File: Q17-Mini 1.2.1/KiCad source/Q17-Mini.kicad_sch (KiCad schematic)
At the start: 86 parts, among them J1 Input, J2-1 SPK+, J2-2 SPK-, J3-1 V+, J3-2 GND, J3-3 V-, Q1 IRF610, Q10 KSA992, Q11 ZVP2106A, Q12 BD139, Q13 IRF610, Q14 IRF9610, Q15 FQA46N15, Q16 FQA36P15, Q2 KSA992, Q3 KSC1845, Q4 IRF9610, Q5 FQP3P20, Q6 FQP3N30, Q7 KSC1845, Q8 ZVN4206AV, Q9 ZVP2106A, U1 OPA1641

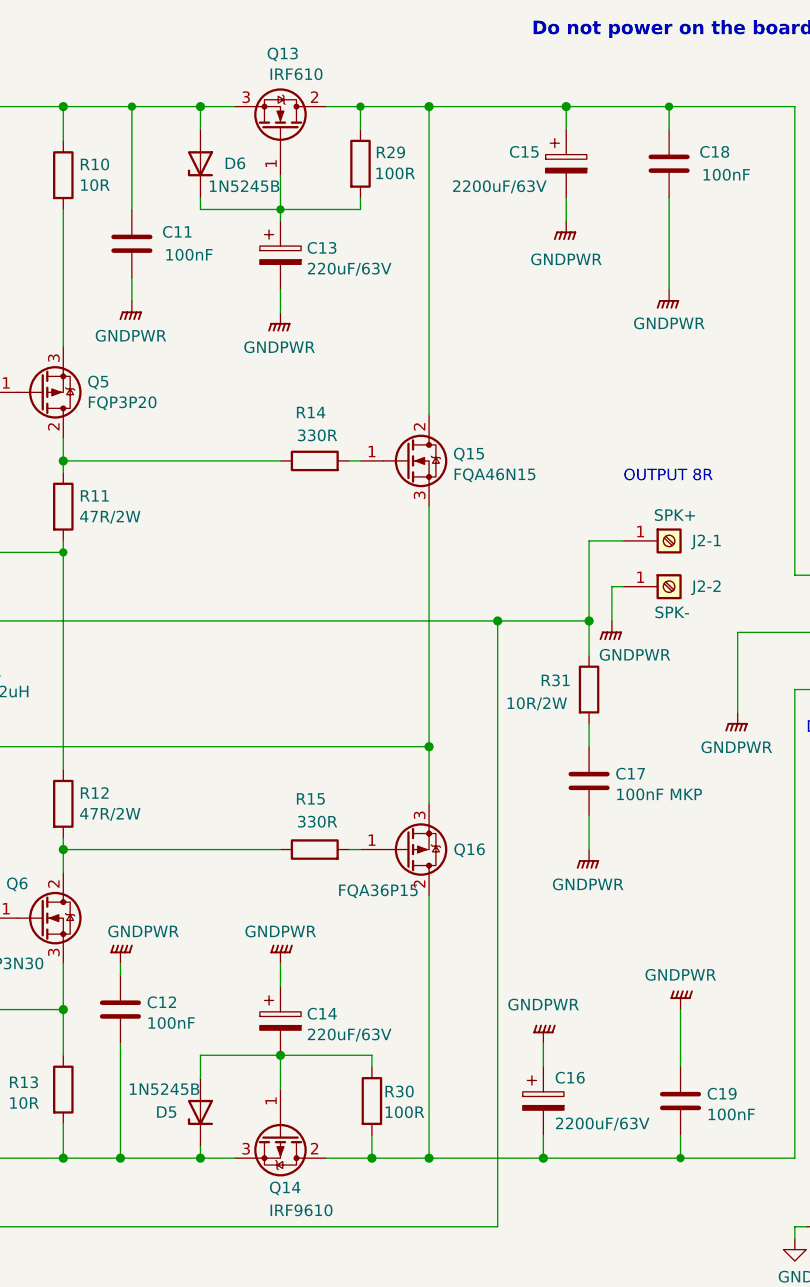
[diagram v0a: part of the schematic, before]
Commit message: Update diagram to 1.3.6
R29/R30 updated to 10k.
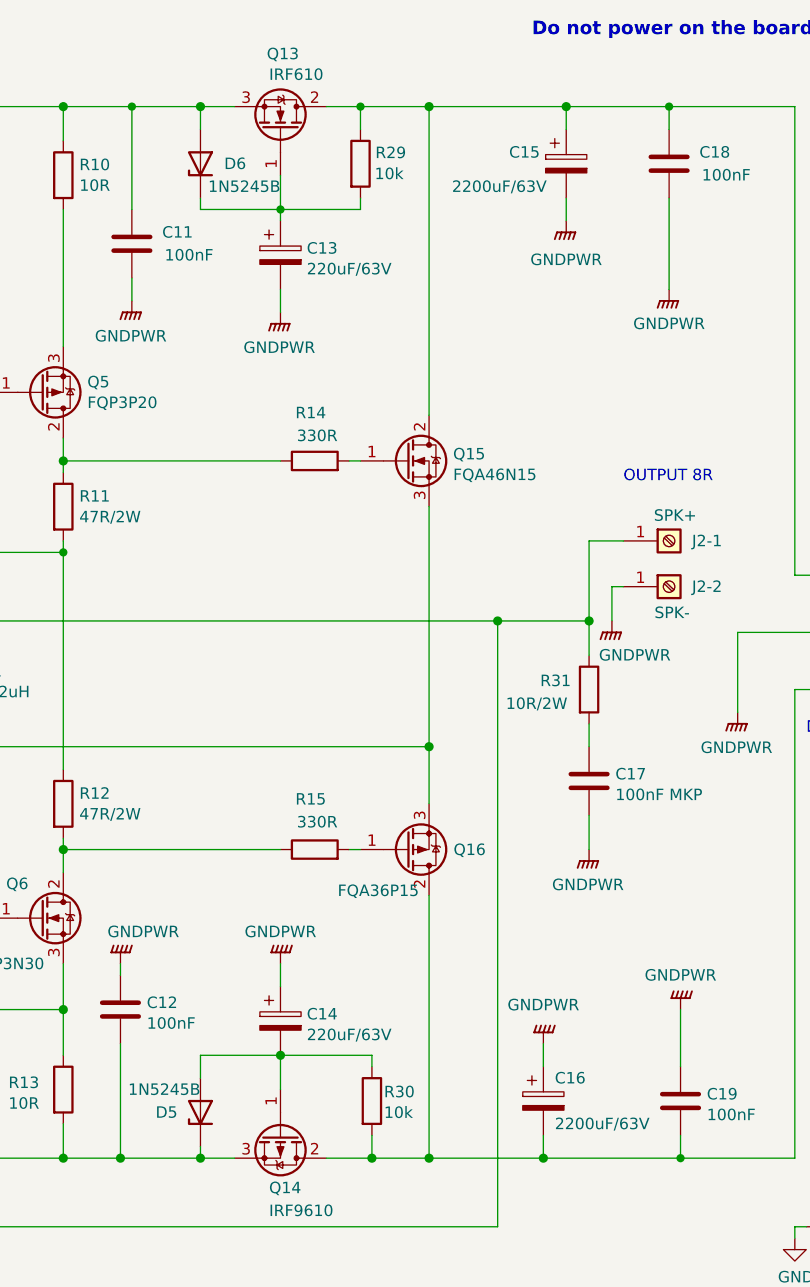
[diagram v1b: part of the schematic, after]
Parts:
- R29, R30: value 100R -> 10k; Part# MRS25000C1000FC100 -> MRS25000C1002FCT00
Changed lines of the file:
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@@
   (title_block
     (title "Q17-Mini Amplifier")
-    (date "2022-08-09")
-    (rev "1.3.5")
+    (date "2022-08-18")
+    (rev "1.3.6")
     (company "by eng. Tiberiu Vicol")
     (comment 1 "Modified by Stef for the Q17-Mini project")
@@
       (effects (font (size 1.27 1.27)) (justify left))
     )
-    (property "Value" "100R" (id 1) (at 216.2005 31.5986 0)
+    (property "Value" "10k" (id 1) (at 216.2005 31.5986 0)
       (effects (font (size 1.27 1.27)) (justify left))
     )
@@
       (effects (font (size 1.27 1.27)) hide)
     )
-    (property "Part#" "MRS25000C1000FC100" (id 4) (at 214.63 30.48 0)
+    (property "Part#" "MRS25000C1002FCT00" (id 4) (at 214.63 30.48 0)
       (effects (font (size 1.27 1.27)) hide)
     )
@@
       (effects (font (size 1.27 1.27)) (justify left))
     )
-    (property "Value" "100R" (id 1) (at 217.2359 135.9102 0)
+    (property "Value" "10k" (id 1) (at 217.2359 135.9102 0)
       (effects (font (size 1.27 1.27)) (justify left))
     )
@@
       (effects (font (size 1.27 1.27)) hide)
     )
-    (property "Part#" "MRS25000C1000FC100" (id 4) (at 215.9 134.62 0)
+    (property "Part#" "MRS25000C1002FCT00" (id 4) (at 215.9 134.62 0)
       (effects (font (size 1.27 1.27)) hide)
     )
@@
     )
     (path "/6a502bca-5c03-4909-9915-ce87906e504a"
-      (reference "R29") (unit 1) (value "100R") (footprint "Resistor_THT:R_Axial_DIN0207_L6.3mm_D2.5mm_P10.16mm_Horizontal")
+      (reference "R29") (unit 1) (value "10k") (footprint "Resistor_THT:R_Axial_DIN0207_L6.3mm_D2.5mm_P10.16mm_Horizontal")
     )
     (path "/860cc2f6-176f-4935-b38a-f52437fa5513"
-      (reference "R30") (unit 1) (value "100R") (footprint "Resistor_THT:R_Axial_DIN0207_L6.3mm_D2.5mm_P10.16mm_Horizontal")
+      (reference "R30") (unit 1) (value "10k") (footprint "Resistor_THT:R_Axial_DIN0207_L6.3mm_D2.5mm_P10.16mm_Horizontal")
     )
     (path "/0b38258b-fc2c-4616-935a-ea7f37c299ab"

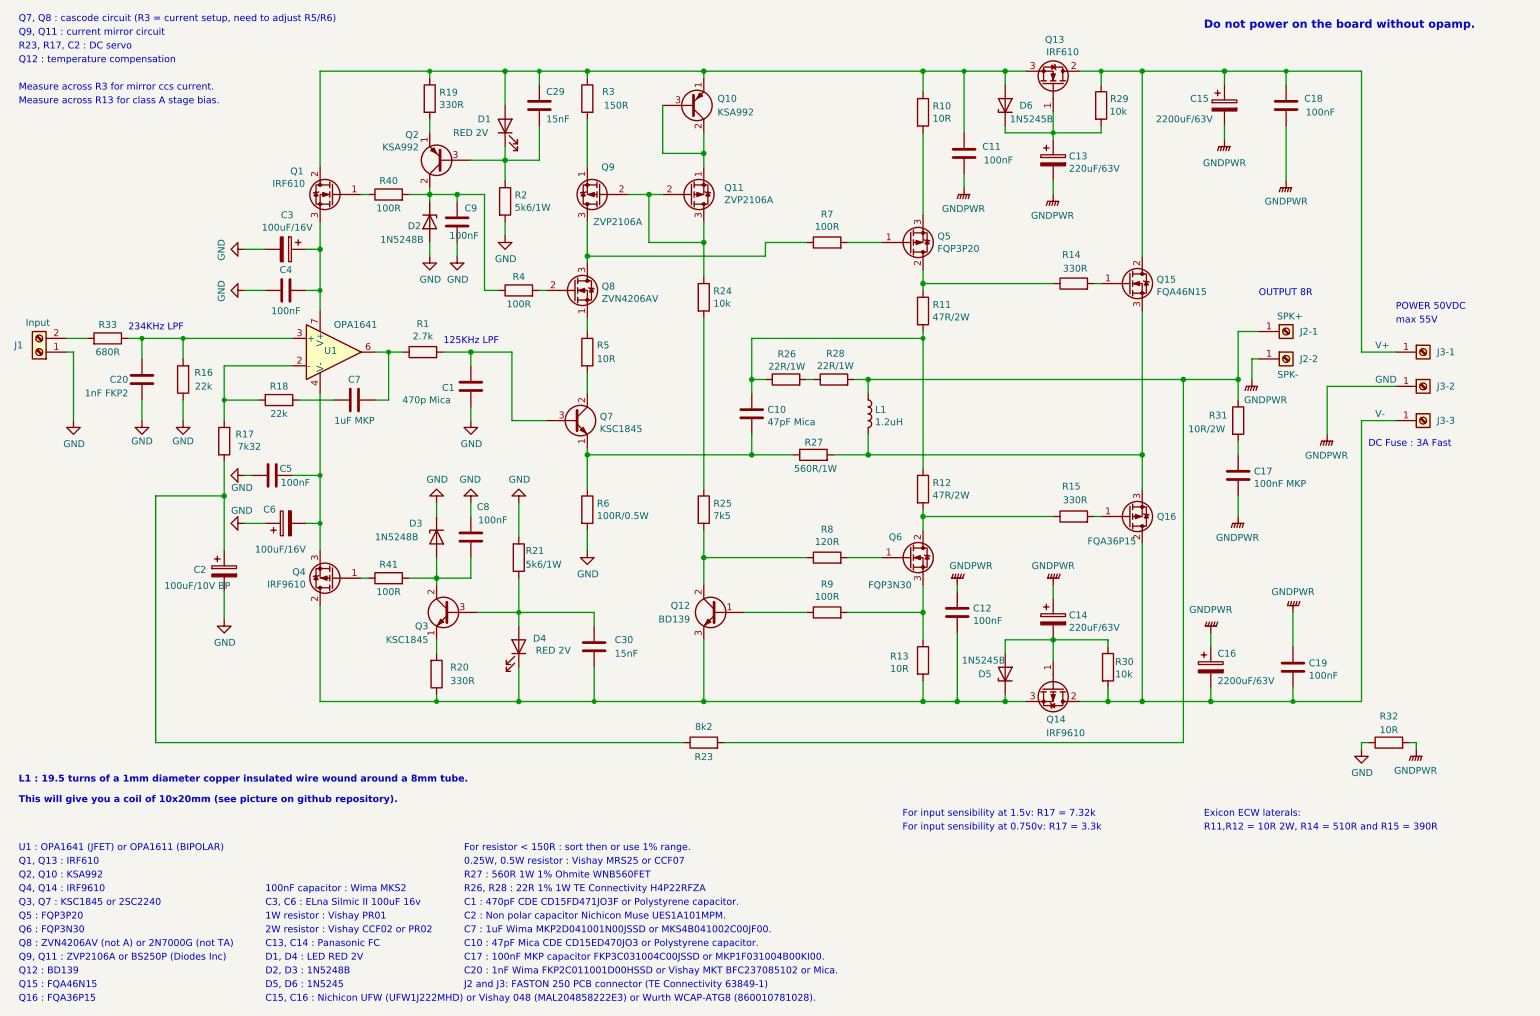
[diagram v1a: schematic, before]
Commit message: Update Q17-Mini 1.2.1
Updated schematic.
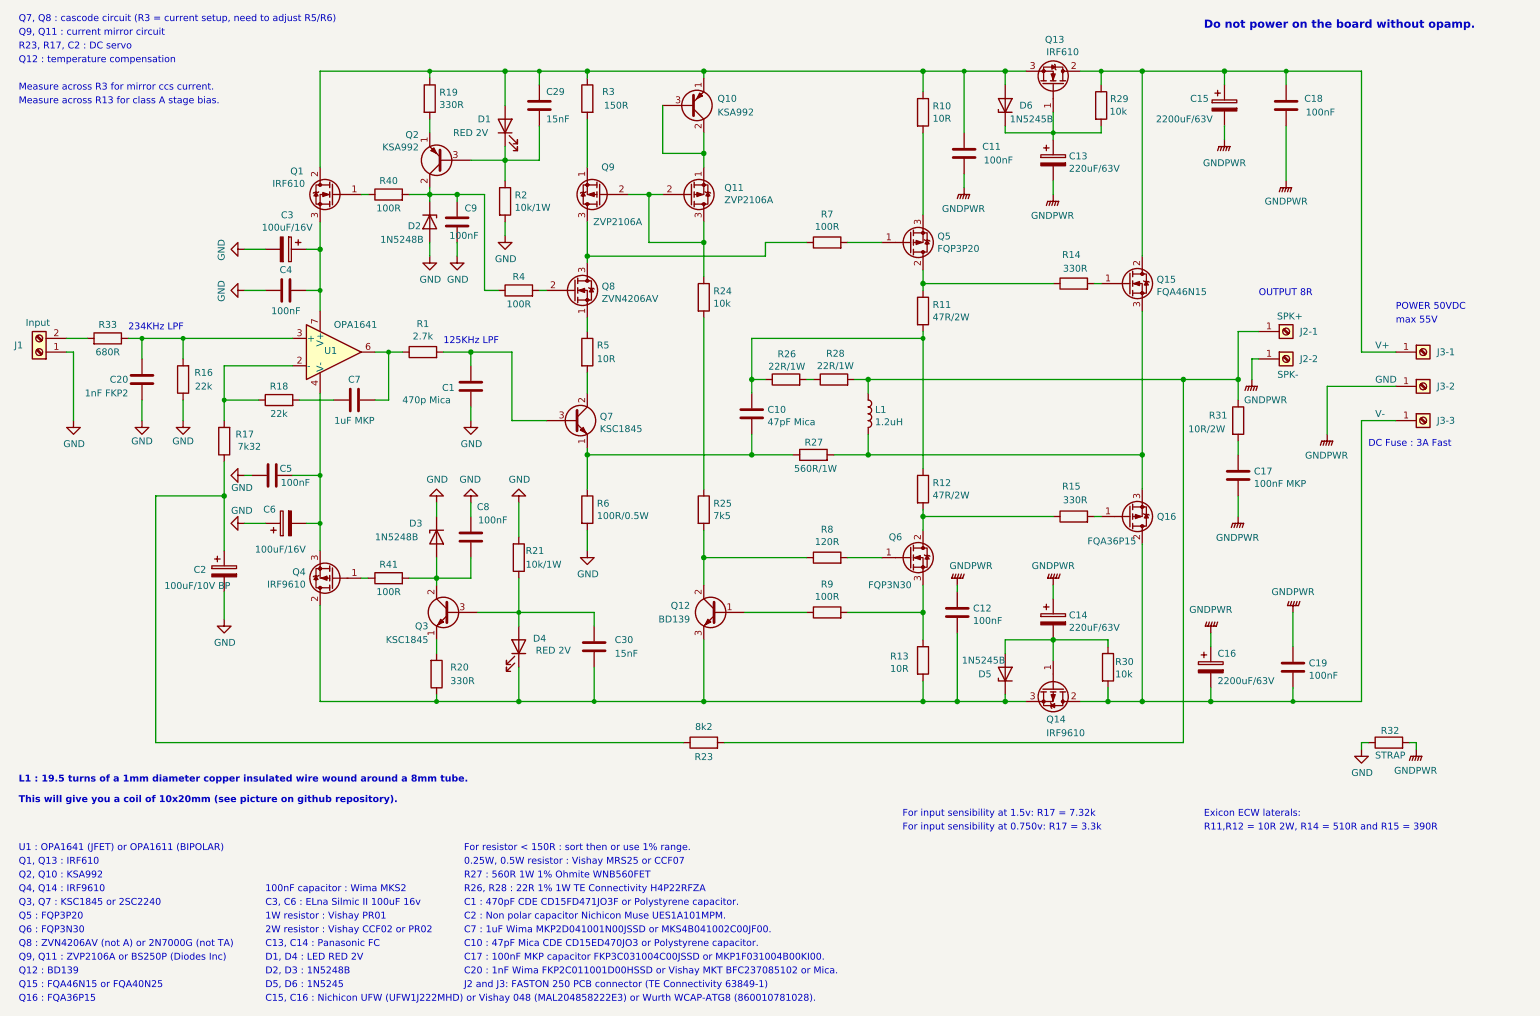
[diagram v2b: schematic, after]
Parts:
- R2, R21: value 5k6/1W -> 10k/1W; Part# PR01000105601JR500 -> PR01000101002JR500
- R32: value 10R -> STRAP
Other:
- note added: "Q15 : FQA46N15 or FQA40N25"
- note removed: "Q15 : FQA46N15"
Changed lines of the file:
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@@
   (title_block
     (title "Q17-Mini Amplifier")
-    (date "2022-08-18")
-    (rev "1.3.6")
+    (date "2022-08-23")
+    (rev "1.3.7")
     (company "by eng. Tiberiu Vicol")
     (comment 1 "Modified by Stef for the Q17-Mini project")
@@
     (effects (font (size 1.27 1.27)) (justify left bottom))
   )
-  (text "Q15 : FQA46N15" (at 13.97 194.31 0)
+  (text "Q15 : FQA46N15 or FQA40N25" (at 13.97 194.31 0)
     (effects (font (size 1.27 1.27)) (justify left bottom))
   )
@@
       (effects (font (size 1.27 1.27)) (justify left))
     )
-    (property "Value" "5k6/1W" (id 1) (at 107.95 115.57 0)
+    (property "Value" "10k/1W" (id 1) (at 107.95 115.57 0)
       (effects (font (size 1.27 1.27)) (justify left))
     )
@@
       (effects (font (size 1.27 1.27)) hide)
     )
-    (property "Part#" "PR01000105601JR500" (id 4) (at 106.68 114.3 0)
+    (property "Part#" "PR01000101002JR500" (id 4) (at 106.68 114.3 0)
       (effects (font (size 1.27 1.27)) hide)
     )
@@
       (effects (font (size 1.27 1.27)) (justify left))
     )
-    (property "Value" "5k6/1W" (id 1) (at 105.918 49.409 0)
+    (property "Value" "10k/1W" (id 1) (at 105.918 49.409 0)
       (effects (font (size 1.27 1.27)) (justify left))
     )
@@
       (effects (font (size 1.27 1.27)) hide)
     )
-    (property "Part#" "PR01000105601JR500" (id 4) (at 104.14 48.26 0)
+    (property "Part#" "PR01000101002JR500" (id 4) (at 104.14 48.26 0)
       (effects (font (size 1.27 1.27)) hide)
     )
@@
   (symbol (lib_id "Device:R") (at 267.97 148.59 90) (unit 1)
     (in_bom yes) (on_board yes)
-    (property "Reference" "R32" (id 0) (at 269.6817 143.7028 90)
+    (property "Reference" "R32" (id 0) (at 269.8898 146.3749 90)
       (effects (font (size 1.27 1.27)) (justify left))
     )
-    (property "Value" "10R" (id 1) (at 269.6817 146.2428 90)
+    (property "Value" "STRAP" (id 1) (at 271.0339 150.951 90)
       (effects (font (size 1.27 1.27)) (justify left))
     )
@@
     )
     (path "/66629faf-a191-4328-8001-bb82d5d2442f"
-      (reference "R2") (unit 1) (value "5k6/1W") (footprint "Resistor_THT:R_Axial_DIN0207_L6.3mm_D2.5mm_P10.16mm_Horizontal")
+      (reference "R2") (unit 1) (value "10k/1W") (footprint "Resistor_THT:R_Axial_DIN0207_L6.3mm_D2.5mm_P10.16mm_Horizontal")
     )
     (path "/86507d1a-5f15-441f-9633-93c496bb3e70"
@@
     )
     (path "/1b488199-e780-425b-bf65-6607168f9f34"
-      (reference "R21") (unit 1) (value "5k6/1W") (footprint "Resistor_THT:R_Axial_DIN0207_L6.3mm_D2.5mm_P10.16mm_Horizontal")
+      (reference "R21") (unit 1) (value "10k/1W") (footprint "Resistor_THT:R_Axial_DIN0207_L6.3mm_D2.5mm_P10.16mm_Horizontal")
     )
     (path "/ee7cc794-8b46-4e6d-a64c-3ff4ac2fc69d"
@@
     )
     (path "/f62732fe-8027-4c0c-a9a9-204da2bf2115"
-      (reference "R32") (unit 1) (value "10R") (footprint "Resistor_THT:R_Axial_DIN0207_L6.3mm_D2.5mm_P10.16mm_Horizontal")
+      (reference "R32") (unit 1) (value "STRAP") (footprint "Resistor_THT:R_Axial_DIN0207_L6.3mm_D2.5mm_P10.16mm_Horizontal")
     )
     (path "/02255283-2707-4e92-96ff-96f5779d9534"
